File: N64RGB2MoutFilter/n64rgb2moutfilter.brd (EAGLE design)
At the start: 123.7 x 29.5 mm, 35 parts

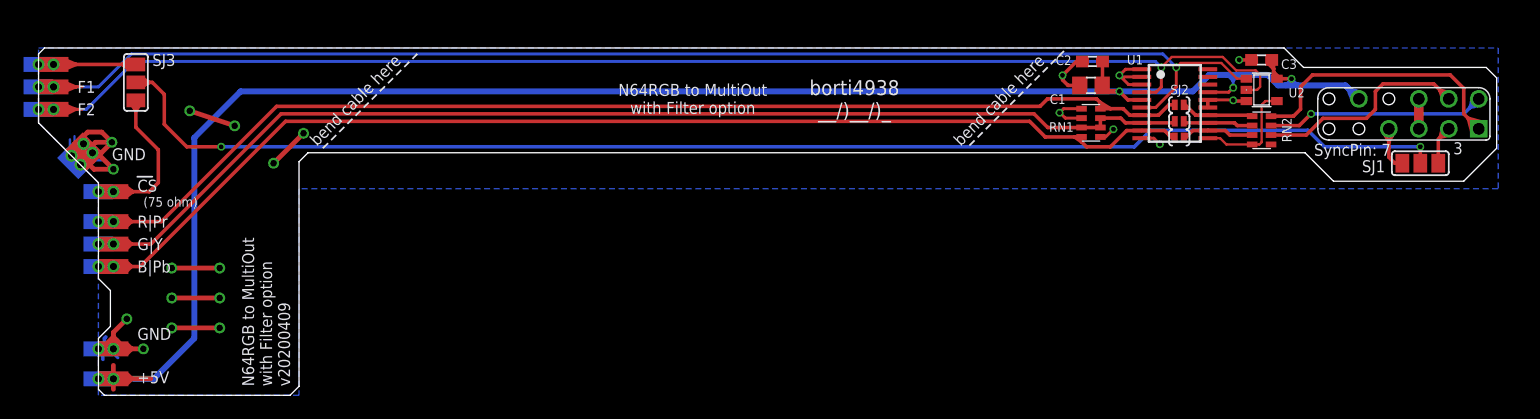
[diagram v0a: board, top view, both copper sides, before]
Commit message: update flex n64rgb2moutfilter to v20211030: - add sync jumper matrix - remove panel file and gerber
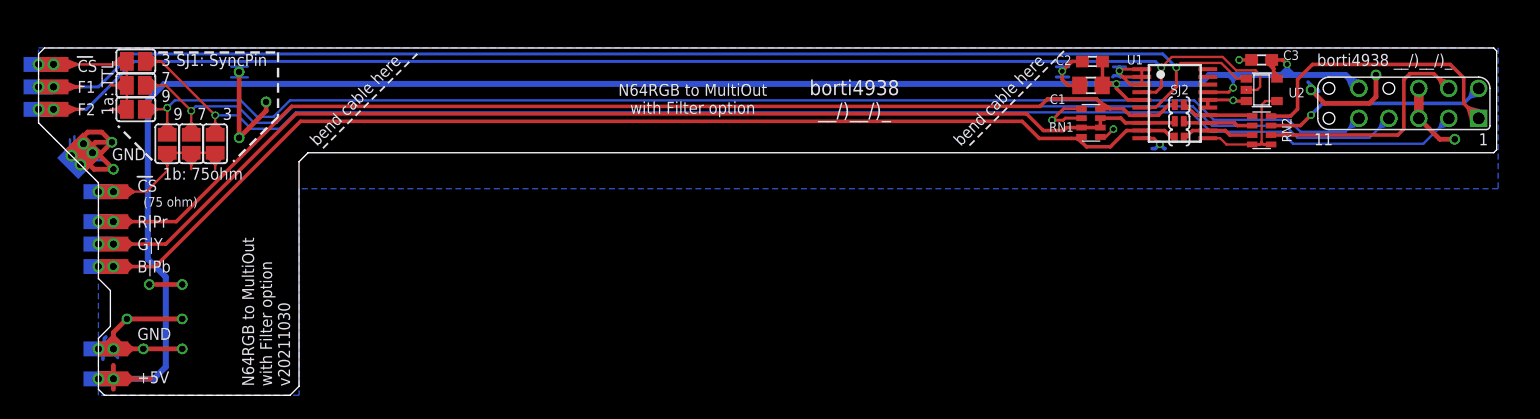
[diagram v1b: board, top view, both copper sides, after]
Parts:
- removed SJ1, SJ3: (no value), jumper:SJ_2
- added E$2, E$3, E$4, E$5, E$6, E$7: (no value), jumper:SJ
- E$1: device snes_div:SNES_MULTIAV_RGBSY -> snes_div:SNES_MULTIAV_RGBSYFBAS
- moved E$1 0.89 mm to (115.8, 24.9)
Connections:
- removed net #CS.SEL: SJ1.2, SJ3.2
- new net FBAS: E$1.9, E$4.2, E$5.2
- net #CS: now also E$2.2, E$7.2; no longer SJ1.1
- net #CS.75.I: now also E$5.1, E$6.1, E$7.1; no longer SJ3.3
- net #CS.I: now also E$2.1, E$3.1, E$4.1; no longer SJ3.1
- net BYPASS_SF: now also RN2.5
- net LUMA: now also E$3.2, E$6.2; no longer SJ1.3
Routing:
- net #CS: track 5.38 -> 126.6 mm, vias 0 -> 1
- net FBAS: track 0.00 -> 117.3 mm, vias 0 -> 1
- net #CS.SEL: track 116.8 -> 0.00 mm, vias 2 -> 0
- net LUMA: track 5.81 -> 121.1 mm, vias 0 -> 1
- net GND: track 84.7 -> 113.0 mm
- net #CS.75.I: track 18.8 -> 33.3 mm
- net #CS.I: track 13.2 -> 26.6 mm
- net 5V: track 155.4 -> 162.1 mm
- net BLUE.OUT.75: track 20.7 -> 22.6 mm
- net BYPASS_SF: track 9.47 -> 10.7 mm
- net RED.OUT.75: track 26.2 -> 27.0 mm
- net BLUE: track 103.6 -> 103.0 mm
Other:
- outline, holes or cut-outs redrawn
- board text added: "1"
- board text added: "11"
- board text added: "1a: TTL"
- board text added: "1b: 75ohm"
- board text added: "9"
- board text added: "Flex-PCB (c) 2019 - 2021 Peter Bartmann"
- board text added: "N64RGB to MultiOut with Filter option v20211030"
- board text added: "SJ1: SyncPin"
- board text removed: "Flex-PCB (c) 2019, 2020 Peter Bartmann"
- board text removed: "N64RGB to MultiOut with Filter option v20200409"
- board text removed: "SyncPin:"
